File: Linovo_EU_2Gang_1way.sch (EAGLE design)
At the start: 41 parts, among them IC1 ATMEGA328P, U1 ATSHA204A, U2 RFM69_MINIMAL

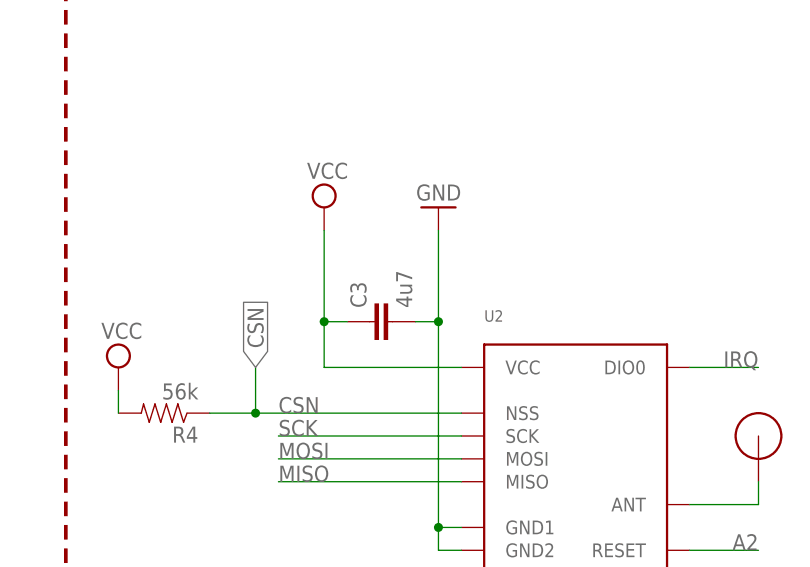
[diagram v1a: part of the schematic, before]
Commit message: Change value RFM69 capacitor
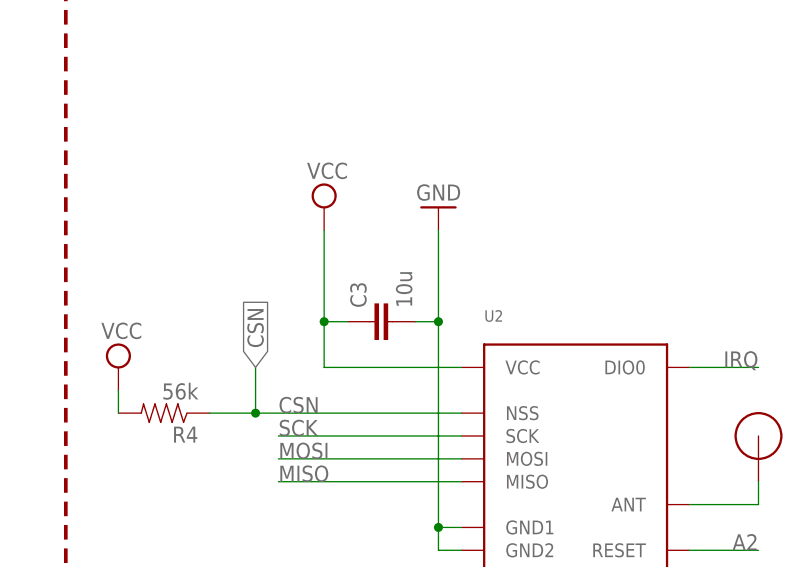
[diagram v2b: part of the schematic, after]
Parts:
- C3: value 4u7 -> 10u
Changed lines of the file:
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@@
 <grid distance="0.1" unitdist="inch" unit="inch" style="lines" multiple="1" display="no" altdistance="0.01" altunitdist="inch" altunit="inch"/>
 <layers>
-<layer number="1" name="Top" color="4" fill="1" visible="yes" active="no"/>
-<layer number="16" name="Bottom" color="1" fill="1" visible="yes" active="no"/>
-<layer number="17" name="Pads" color="2" fill="1" visible="yes" active="no"/>
-<layer number="18" name="Vias" color="2" fill="1" visible="yes" active="no"/>
-<layer number="19" name="Unrouted" color="6" fill="1" visible="yes" active="no"/>
-<layer number="20" name="Dimension" color="15" fill="1" visible="yes" active="no"/>
-<layer number="21" name="tPlace" color="7" fill="1" visible="yes" active="no"/>
-<layer number="22" name="bPlace" color="7" fill="1" visible="yes" active="no"/>
-<layer number="23" name="tOrigins" color="15" fill="1" visible="yes" active="no"/>
-<layer number="24" name="bOrigins" color="15" fill="1" visible="yes" active="no"/>
-<layer number="25" name="tNames" color="7" fill="1" visible="yes" active="no"/>
-<layer number="26" name="bNames" color="7" fill="1" visible="yes" active="no"/>
-<layer number="27" name="tValues" color="7" fill="1" visible="yes" active="no"/>
-<layer number="28" name="bValues" color="7" fill="1" visible="yes" active="no"/>
+<layer number="1" name="Top" color="4" fill="1" visible="no" active="no"/>
+<layer number="16" name="Bottom" color="1" fill="1" visible="no" active="no"/>
+<layer number="17" name="Pads" color="2" fill="1" visible="no" active="no"/>
+<layer number="18" name="Vias" color="2" fill="1" visible="no" active="no"/>
+<layer number="19" name="Unrouted" color="6" fill="1" visible="no" active="no"/>
+<layer number="20" name="Dimension" color="15" fill="1" visible="no" active="no"/>
+<layer number="21" name="tPlace" color="7" fill="1" visible="no" active="no"/>
+<layer number="22" name="bPlace" color="7" fill="1" visible="no" active="no"/>
+<layer number="23" name="tOrigins" color="15" fill="1" visible="no" active="no"/>
+<layer number="24" name="bOrigins" color="15" fill="1" visible="no" active="no"/>
+<layer number="25" name="tNames" color="7" fill="1" visible="no" active="no"/>
+<layer number="26" name="bNames" color="7" fill="1" visible="no" active="no"/>
+<layer number="27" name="tValues" color="7" fill="1" visible="no" active="no"/>
+<layer number="28" name="bValues" color="7" fill="1" visible="no" active="no"/>
 <layer number="29" name="tStop" color="7" fill="3" visible="no" active="no"/>
 <layer number="30" name="bStop" color="7" fill="6" visible="no" active="no"/>
@@
 <layer number="35" name="tGlue" color="7" fill="4" visible="no" active="no"/>
 <layer number="36" name="bGlue" color="7" fill="5" visible="no" active="no"/>
-<layer number="37" name="tTest" color="7" fill="1" visible="yes" active="no"/>
-<layer number="38" name="bTest" color="7" fill="1" visible="yes" active="no"/>
+<layer number="37" name="tTest" color="7" fill="1" visible="no" active="no"/>
+<layer number="38" name="bTest" color="7" fill="1" visible="no" active="no"/>
 <layer number="39" name="tKeepout" color="4" fill="11" visible="no" active="no"/>
 <layer number="40" name="bKeepout" color="1" fill="11" visible="no" active="no"/>
@@
 <layer number="44" name="Drills" color="7" fill="1" visible="no" active="no"/>
 <layer number="45" name="Holes" color="7" fill="1" visible="no" active="no"/>
-<layer number="46" name="Milling" color="3" fill="1" visible="yes" active="no"/>
-<layer number="47" name="Measures" color="7" fill="1" visible="yes" active="no"/>
-<layer number="48" name="Document" color="7" fill="1" visible="yes" active="no"/>
-<layer number="49" name="Reference" color="7" fill="1" visible="yes" active="no"/>
-<layer number="50" name="dxf" color="7" fill="1" visible="yes" active="no"/>
-<layer number="51" name="tDocu" color="7" fill="1" visible="yes" active="no"/>
-<layer number="52" name="bDocu" color="7" fill="1" visible="yes" active="no"/>
-<layer number="53" name="tGND_GNDA" color="7" fill="1" visible="yes" active="no"/>
-<layer number="54" name="bGND_GNDA" color="7" fill="1" visible="yes" active="no"/>
-<layer number="56" name="wert" color="7" fill="1" visible="yes" active="no"/>
-<layer number="57" name="tCAD" color="7" fill="1" visible="yes" active="no"/>
-<layer number="58" name="b3D" color="7" fill="1" visible="yes" active="no"/>
-<layer number="59" name="tCarbon" color="7" fill="1" visible="yes" active="no"/>
-<layer number="60" name="bCarbon" color="7" fill="1" visible="yes" active="no"/>
+<layer number="46" name="Milling" color="3" fill="1" visible="no" active="no"/>
+<layer number="47" name="Measures" color="7" fill="1" visible="no" active="no"/>
+<layer number="48" name="Document" color="7" fill="1" visible="no" active="no"/>
+<layer number="49" name="Reference" color="7" fill="1" visible="no" active="no"/>
+<layer number="50" name="dxf" color="7" fill="1" visible="no" active="no"/>
+<layer number="51" name="tDocu" color="7" fill="1" visible="no" active="no"/>
+<layer number="52" name="bDocu" color="7" fill="1" visible="no" active="no"/>
+<layer number="53" name="tGND_GNDA" color="7" fill="1" visible="no" active="no"/>
+<layer number="54" name="bGND_GNDA" color="7" fill="1" visible="no" active="no"/>
+<layer number="56" name="wert" color="7" fill="1" visible="no" active="no"/>
+<layer number="57" name="tCAD" color="7" fill="1" visible="no" active="no"/>
+<layer number="58" name="b3D" color="7" fill="1" visible="no" active="no"/>
+<layer number="59" name="tCarbon" color="7" fill="1" visible="no" active="no"/>
+<layer number="60" name="bCarbon" color="7" fill="1" visible="no" active="no"/>
 <layer number="90" name="Modules" color="5" fill="1" visible="yes" active="yes"/>
 <layer number="91" name="Nets" color="2" fill="1" visible="yes" active="yes"/>
@@
 <part name="SUPPLY5" library="supply2" deviceset="VCC" device=""/>
 <part name="R4" library="LowPowerLab" deviceset="RESISTOR" device="0603-RES" value="56k"/>
-<part name="C3" library="LowPowerLab" deviceset="CAP" device="0603-CAP" value="4u7"/>
+<part name="C3" library="LowPowerLab" deviceset="CAP" device="0603-CAP" value="10u"/>
 <part name="U$3" library="SparkFun" deviceset="RESONATOR" device="SMD" value="8MHZ"/>
 <part name="FRAME1" library="frames" deviceset="A3L-LOC" device=""/>
